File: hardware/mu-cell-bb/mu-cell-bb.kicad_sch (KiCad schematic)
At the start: 81 parts, among them IC1 SX1255IWLTRT, J1 TX, J2 RX, J3 EXT_CLK, J4 RPi GPIO, J5 IO, Q1 BC817-40W, Q2 BC817-40W, U1 24LC256, U2 LDK130M33R, Y1 32MHz

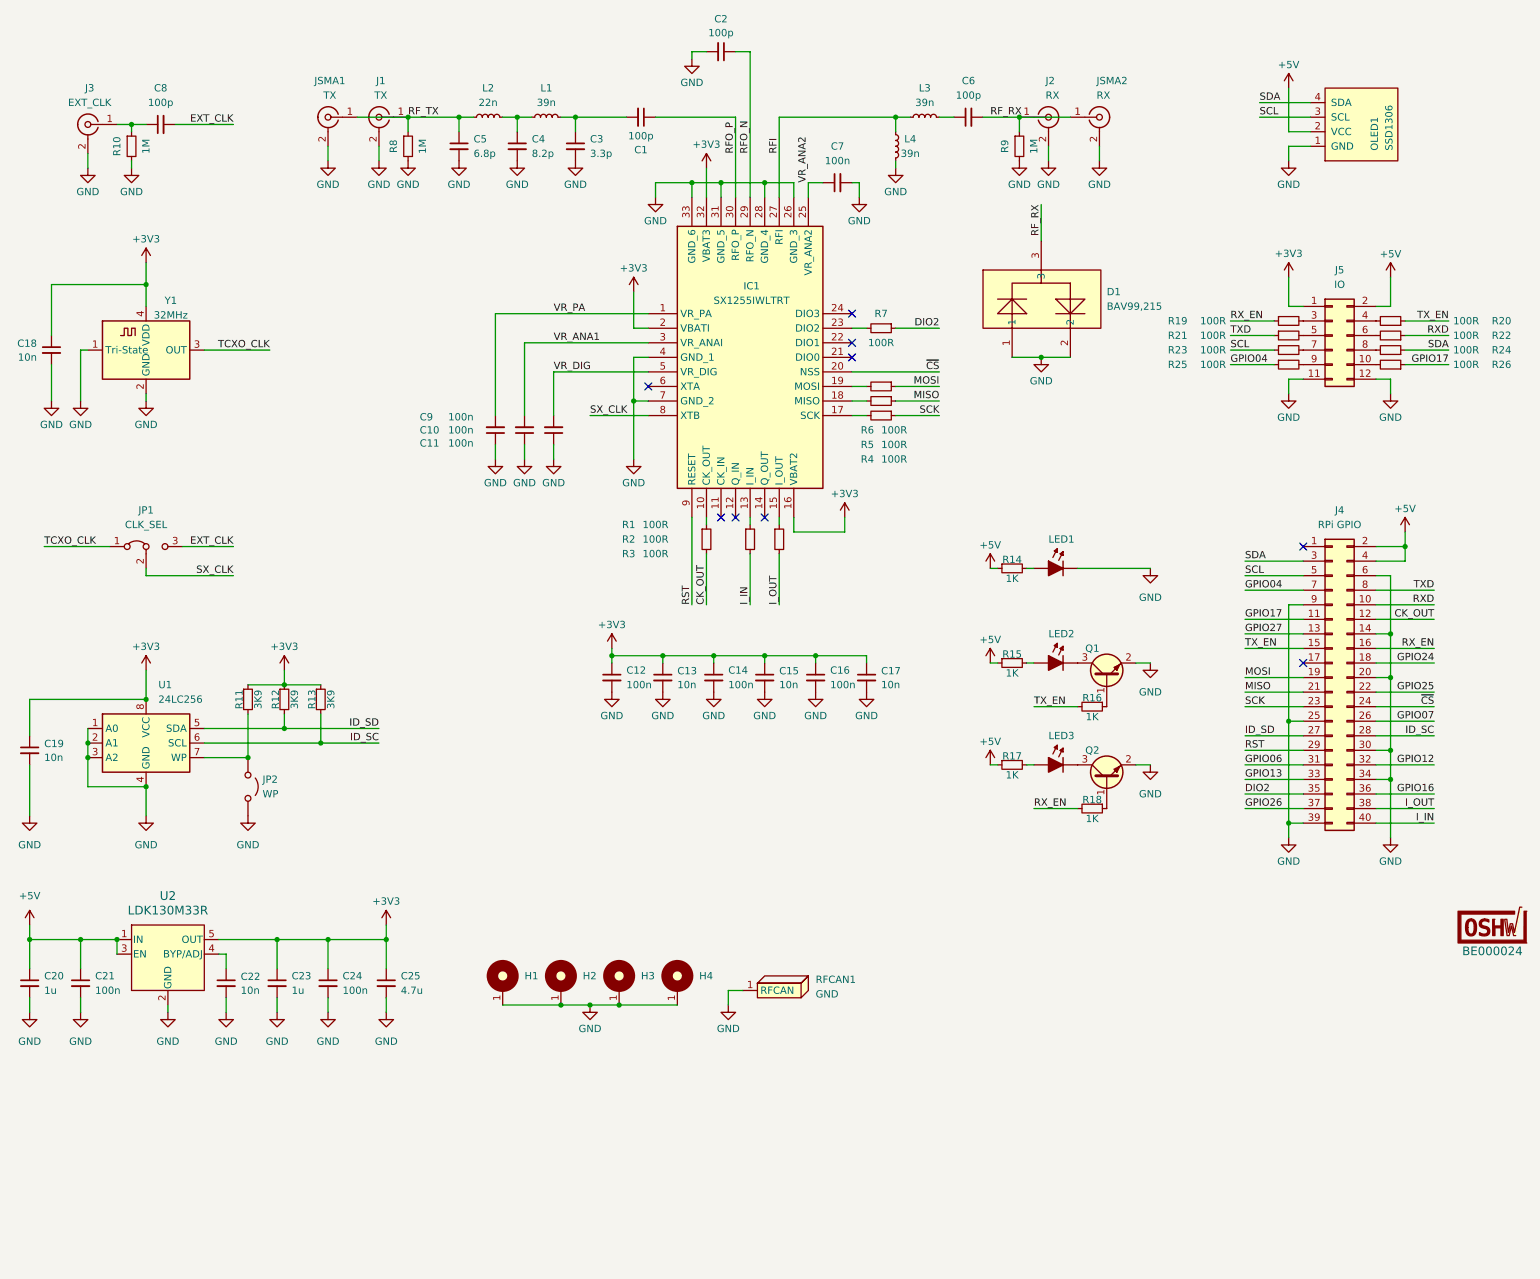
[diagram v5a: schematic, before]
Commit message: added eeprom programming header, updated part numbers
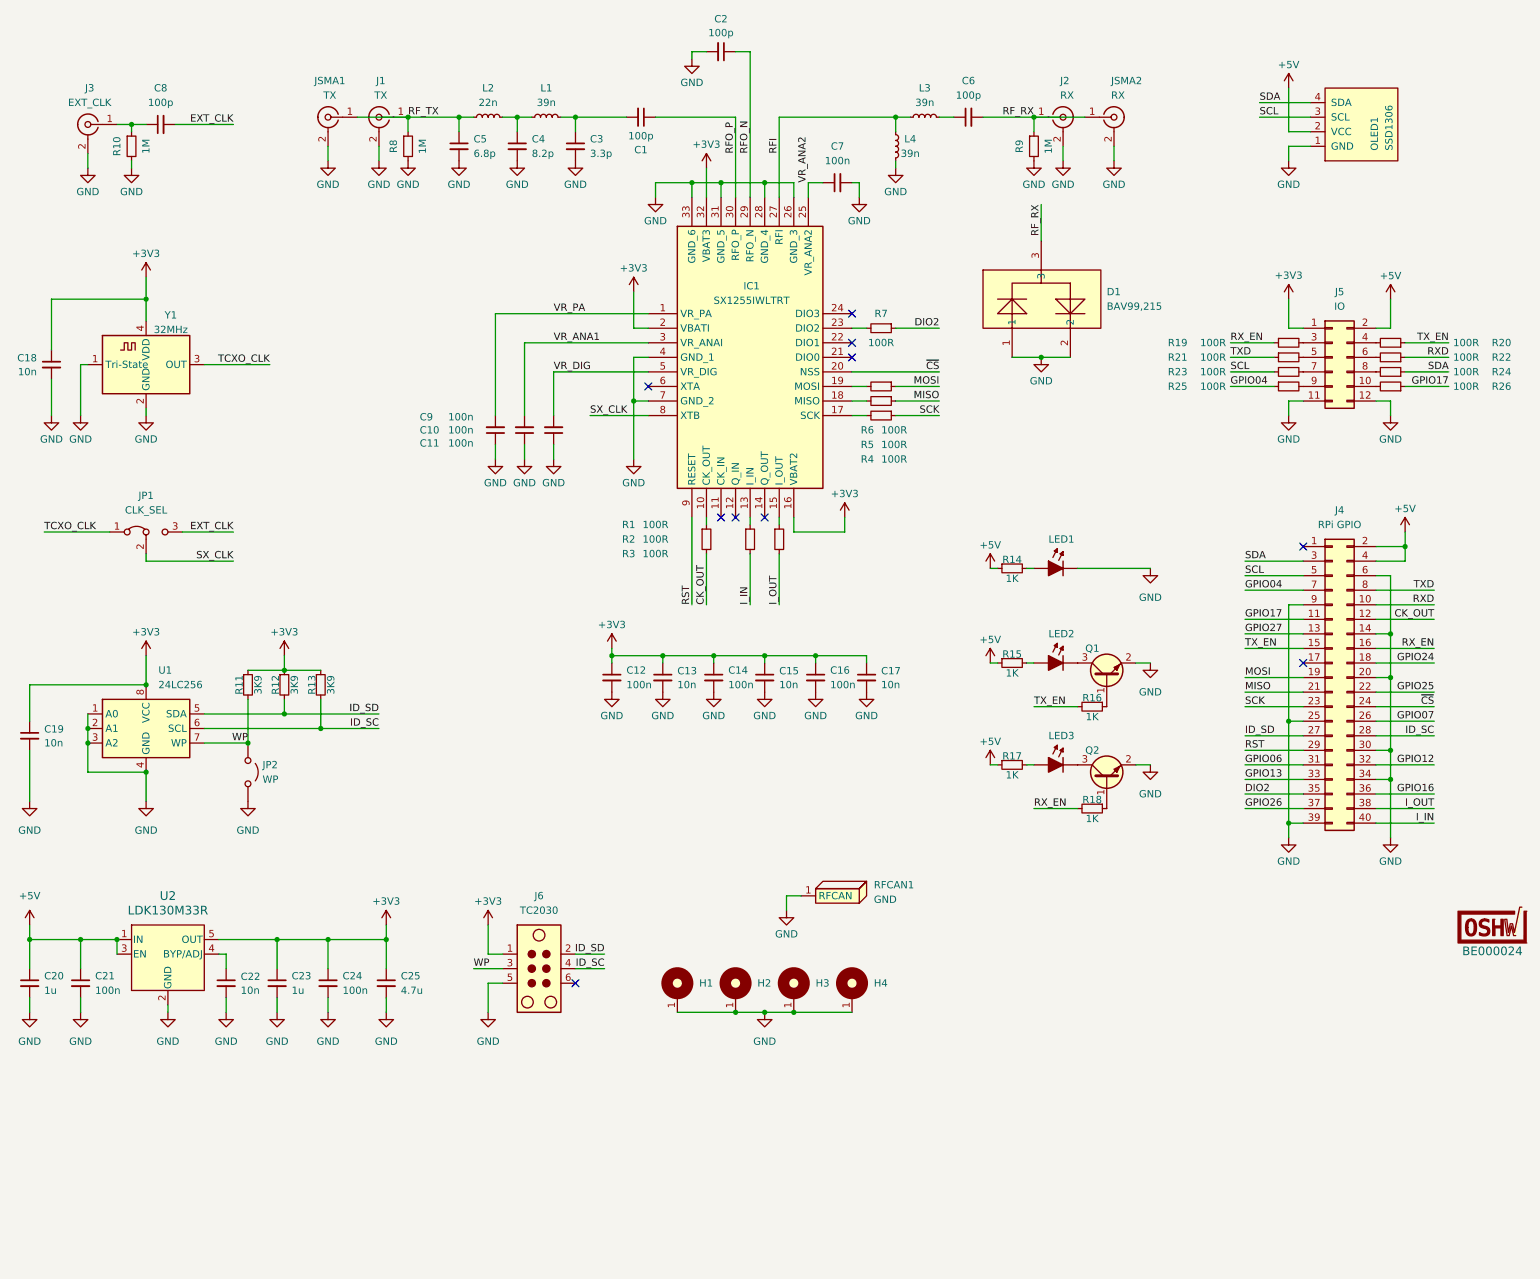
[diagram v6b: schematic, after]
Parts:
- added J6: TC2030, Connector:Tag-Connect_TC2030-IDC-NL_2x03_P1.27mm_Vertical, symbol Connector:TC2030
- LED1: value Green -> Red; LCSC Part (none) -> C7496803
- LED2: value Red -> Amber; LCSC Part (none) -> C5123495
- LED3: value Yellow -> Green; LCSC Part (none) -> C74338
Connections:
- net +3V3: now also J6.1
- net GND: now also J6.5
- net ID_SC: now also J6.4
- net ID_SD: now also J6.2
- net WP: now reaches JP2.1 (A), R11.2, U1.7 (WP)
- net WP: now also J6.3
- no-connect marks 9 -> 10
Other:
- moved on the sheet: C18, C19, H1, H2, H3, H4, J2, J5, JP1, JP2, JSMA2, R11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

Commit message: made final changes before ordering first batch
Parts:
- added J7: TC2030, Connector:Tag-Connect_TC2030-IDC-NL_2x03_P1.27mm_Vertical, symbol Connector:TC2030
- C1, C2: LCSC Part (none) -> C2941926
- C3: LCSC Part (none) -> C2941931
- C4: LCSC Part C1864373 -> C2857971
- L1, L3, L4: LCSC Part (none) -> C40399699
- L2: LCSC Part (none) -> C22440906
- Y1: value 32MHz -> 38.4MHz; LCSC Part C48332760 -> C1987359
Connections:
- net +3V3: now also J7.1
- net GND: now also J7.5
- net ID_SC: now also J7.4
- net ID_SD: now also J7.2
- net RFI: now also D1.3
- net RF_RX: no longer D1.3
- net WP: now also J7.3
- no-connect marks 10 -> 11

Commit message: migrated to KiCAD 10.0
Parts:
- BE000024: value ~ -> (none)
